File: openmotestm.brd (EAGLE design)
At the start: 24.4 x 34 mm, 46 parts, among them X1 PHB_1MM27_2X05_SNS

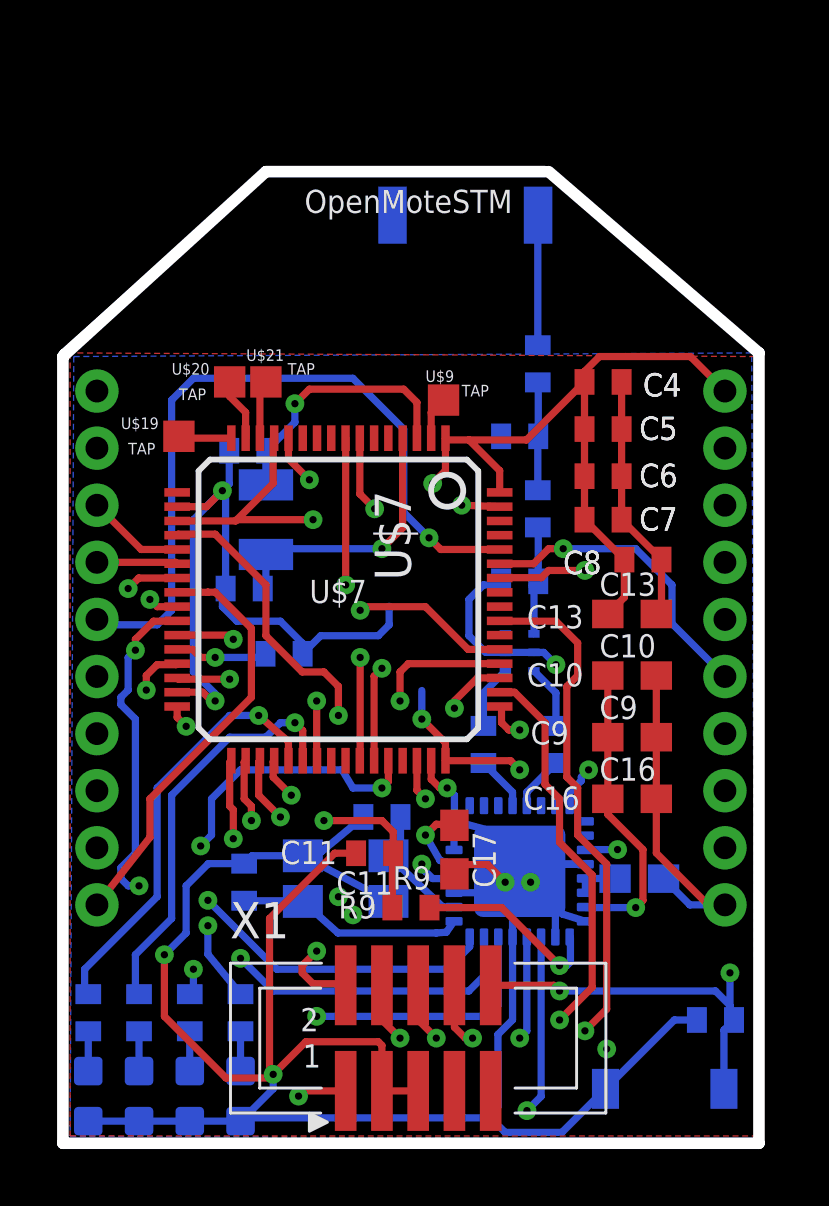
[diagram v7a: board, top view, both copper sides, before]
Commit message: exchange the top layer and bottom layer.
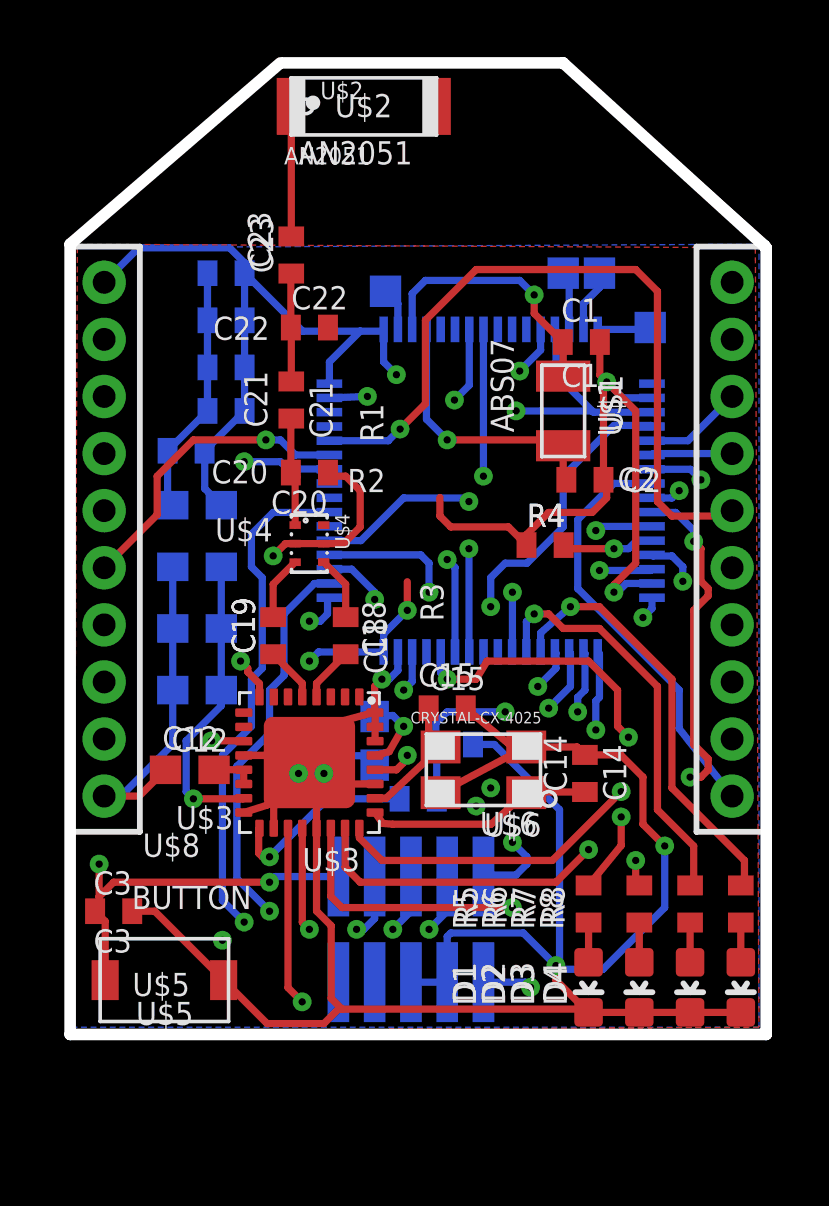
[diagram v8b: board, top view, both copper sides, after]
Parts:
- moved D4 23.2 mm to (12.1, -9.78), flipped to the top
- moved R8 23.2 mm to (12.1, -6.86), flipped to the top
- moved C3 21.4 mm to (-9.91, -7.11), flipped to the top
- moved D3 19.7 mm to (10.3, -9.78), flipped to the top
- moved R7 19.7 mm to (10.3, -6.86), flipped to the top
- moved U$5 17.9 mm to (-8.13, -9.53), flipped to the top
- moved U$19 16.9 mm to (8.89, 13.3), flipped to the bottom
- moved C8 16.4 mm to (-7.37, 9.02), flipped to the bottom
- moved C12 16.2 mm to (-7.24, -2.16), flipped to the top
- moved D2 16.2 mm to (8.51, -9.78), flipped to the top
- moved R6 16.2 mm to (8.51, -6.86), flipped to the top
- moved C10 15.7 mm to (-6.99, 4.95), flipped to the bottom
- moved C13 15.7 mm to (-6.99, 7.11), flipped to the bottom
- moved C16 15.7 mm to (-6.99, 0.64), flipped to the bottom
- moved C9 15.7 mm to (-6.99, 2.79), flipped to the bottom
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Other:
- outline, holes or cut-outs redrawn
